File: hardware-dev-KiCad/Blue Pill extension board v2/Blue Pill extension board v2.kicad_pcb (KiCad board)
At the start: 2 copper layers, 68 x 85 mm, 14 parts, among them J1 NRF_MODULE, J2 Conn_02x20_Odd_Even, J3 SD_CARD, J4 Conn_02x20_Odd_Even, J5 GPS_MODULE, J6 HUM & TEMP SENSOR, U1 YAAJ_BluePill_Part_Like

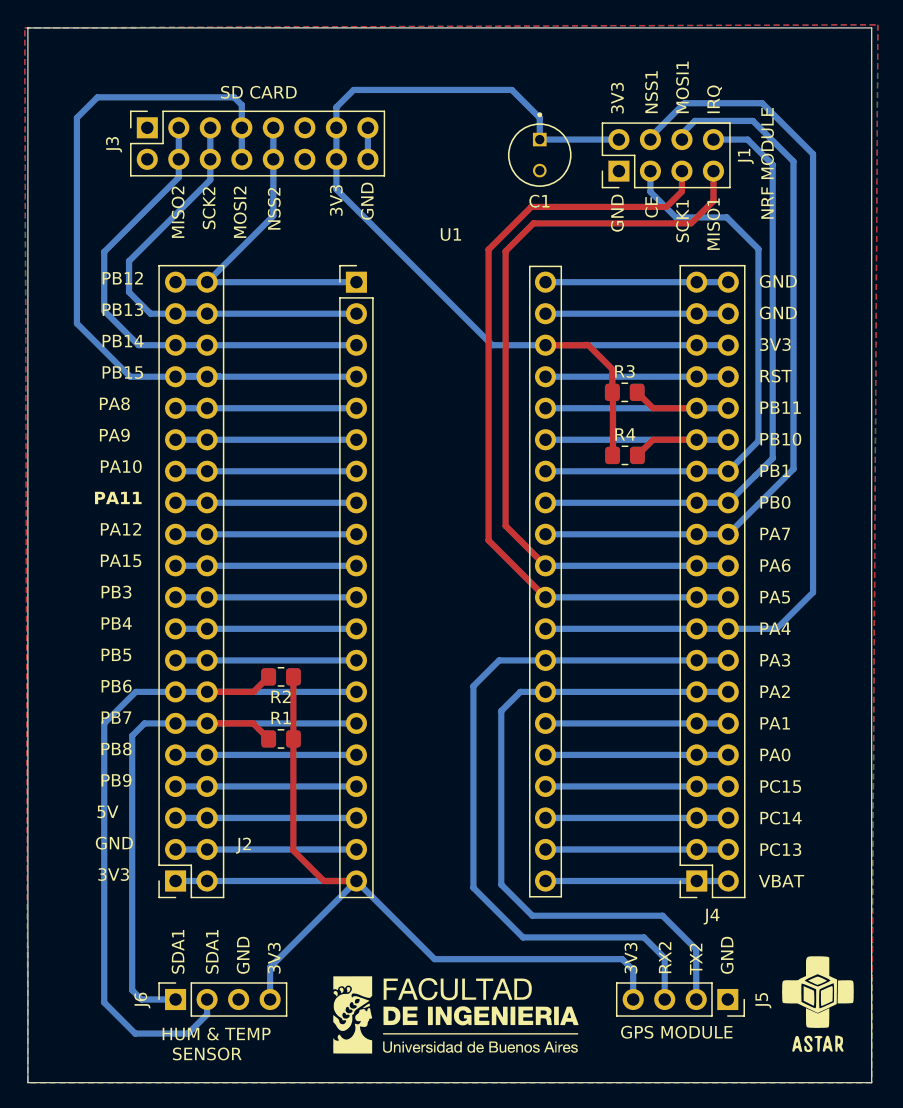
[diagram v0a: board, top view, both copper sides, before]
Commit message: Modifico placa para hacerla de una sola capa
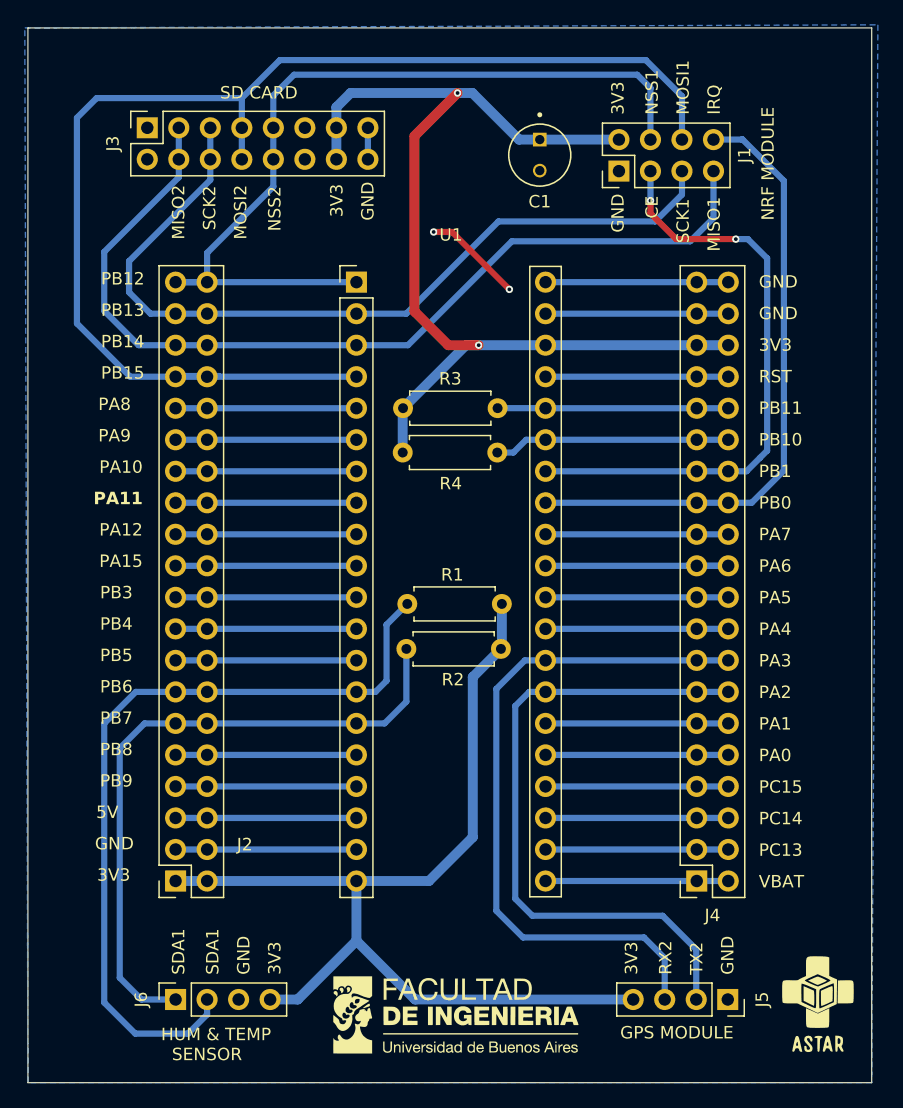
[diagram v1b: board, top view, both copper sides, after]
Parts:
- R1, R2, R3, R4: footprint Resistor_SMD:R_0805_2012Metric_Pad1.20x1.40mm_HandSolder -> Resistor_THT:R_Axial_DIN0207_L6.3mm_D2.5mm_P7.62mm_Horizontal
- moved R2 18.7 mm to (151.0, 92.4)
- moved R4 17.9 mm to (143.0, 80.2)
- moved R3 17.9 mm to (143.0, 76.6)
- moved R1 12.4 mm to (143.3, 96.0)
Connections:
- J1 pad 4: NSS1 -> NSS2
- J1 pad 5: SCK1 -> SCK2
- J1 pad 6: MOSI1 -> MOSI2
- J1 pad 7: MISO1 -> MISO2
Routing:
- net NSS1: track 74.2 -> 14.7 mm
- net SCK1: track 63.8 -> 14.7 mm
- net MISO1: track 65.6 -> 18.1 mm
- net MOSI1: track 58.2 -> 14.7 mm
- net MOSI2: track 63.0 -> 104.7 mm
- net NSS2: track 32.0 -> 70.3 mm
- net MISO2: track 38.7 -> 75.5 mm
- net SCK2: track 35.0 -> 67.1 mm
- net 3V3_L: track 74.7 -> 83.2 mm
- net GND: track 46.6 -> 54.6 mm, vias 0 -> 2
- net SDA1: track 47.7 -> 52.0 mm
- net SCL1: track 60.5 -> 64.8 mm
- net 3V3_R: track 82.6 -> 86.2 mm, vias 0 -> 2
- net RX2: track 58.8 -> 56.0 mm
- net PB1: track 45.9 -> 48.4 mm, vias 0 -> 2
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- removed copper zone on F.Cu, net GND
